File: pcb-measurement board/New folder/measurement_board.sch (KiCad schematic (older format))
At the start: 92 parts, among them P1 HDR DUAL ROW, P2 CONN_02X15, P3 CONN_02X13, P4 CONN_02X05, P5 CONN_02X05, Q1 Si1101X, U1 NX3L4051, U10 TLV1G125, U11 NX3L4051, U12 MSP430G2955, U13 AD8603, U14 TLV1G125, U15 MCP4921, U16 AD8293, U17 NX3L4051, U18 NX3L4051, U19 QS4A110, U2 TPS73133, U20 QS4A110, U21 TLV1G125, U22 TLV1G125, U3 74CBTLV3253, U4 NX3L4051, U5 TPS73125, U6 AD8603, U7 MCP4921, U8 NX3L4051, U9 TLV1G125

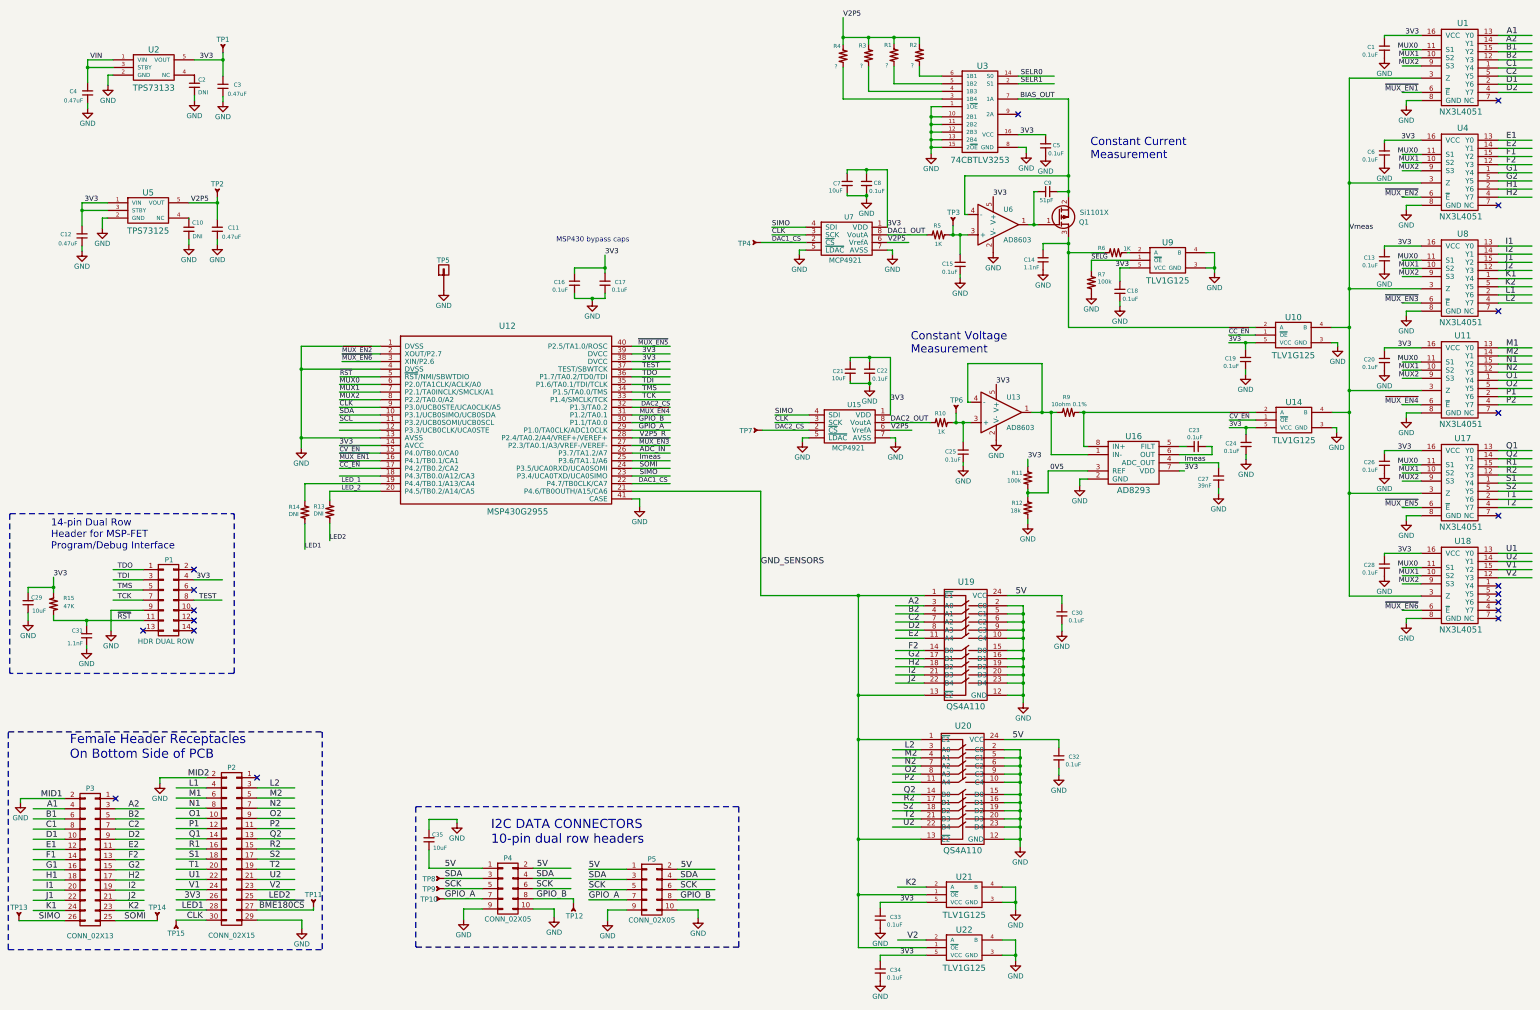
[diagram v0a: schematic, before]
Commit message: -replaced all measurement board 0402 components with 0603 -adjusted placement and started routing on the layout
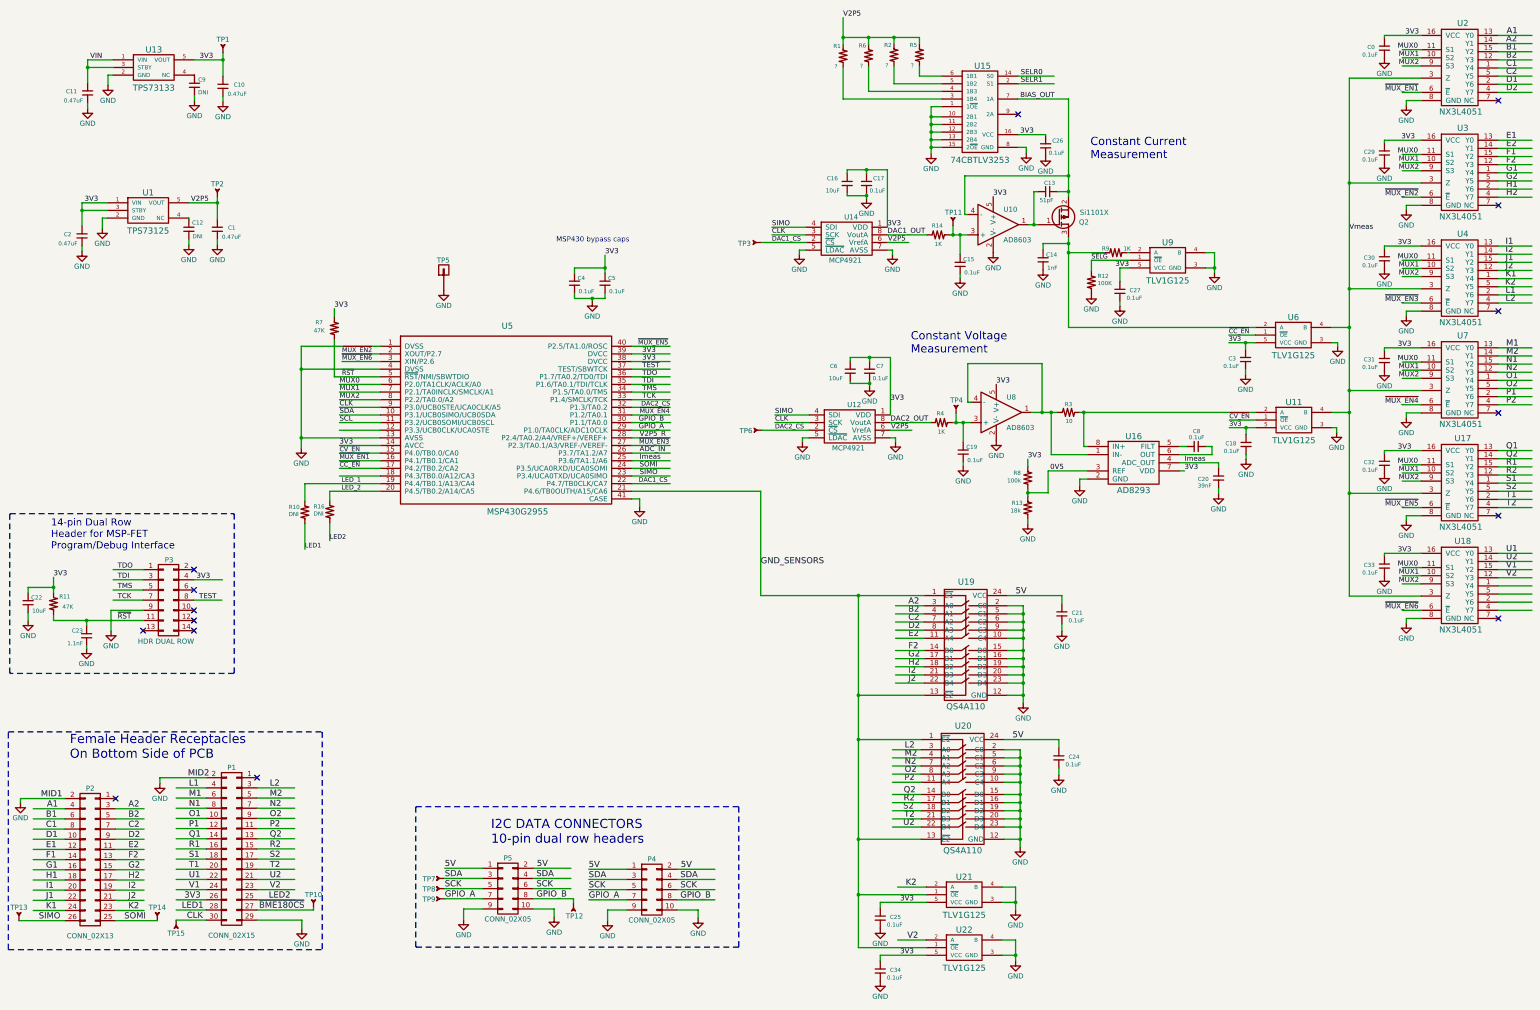
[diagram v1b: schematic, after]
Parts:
- removed C18, C22, C23, C25: 0.1uF, footprints_on_Cdrive:0603, symbol CAP_NP
- removed C21, C35: 10uF, footprints_on_Cdrive:0603, symbol CAP_NP
- removed R15: 47K, footprints_on_Cdrive:0603, symbol Res1_1
- removed R5, R6: 1K, footprints_on_Cdrive:0603, symbol Res1_1
- added C19, C26, C4: 0.1uF, footprints_on_Cdrive:0402, symbol CAP_NP
- added C27: 0.1uF, Resistors_SMD:R_0603_HandSoldering, symbol CAP_NP
- added C6: 10uF, footprints_on_Cdrive:0402, symbol CAP_NP
- added R11: 47K, footprints_on_Cdrive:0402, symbol Res1
- added R12: 100K, footprints_on_Cdrive:0402, symbol Res1_1
- added R14, R9: 1K, footprints_on_Cdrive:0402, symbol Res1_1
- C13: renamed from C9; footprint footprints_on_Cdrive:0603 -> footprints_on_Cdrive:0402; description CAP CER 51PF 50V C0G/NP0 0603 -> CAP CER 51PF 50V NP0 0402; manufacturer pn GRM1885C1H510JA01D -> GRM1555C1H510JA01D; supplier pn 490-1420-1-ND -> 490-5944-1-ND
- C14: value 1.1nF -> 1nF; footprint footprints_on_Cdrive:0603 -> footprints_on_Cdrive:0402; description CAP CER 1100PF 50V C0G/NP0 0603 -> CAP CER 1000PF 50V X7R 0402; manufacturer pn GRM1885C1H112JA01D -> GRM155R71H102KA01D; supplier pn 490-1452-1-ND -> 490-1303-1-ND
- C15, C17, C5, C8: footprint footprints_on_Cdrive:0603 -> footprints_on_Cdrive:0402; description CAP CER 0.1UF 16V X7R 0603 -> CAP CER 0.1UF 16V X5R 0402; manufacturer pn GRM188R71C104KA01D -> 0402YD104KAT2A; supplier pn 490-1532-1-ND -> 478-1126-1-ND
- C16: value 0.1uF -> 10uF; footprint footprints_on_Cdrive:0603 -> footprints_on_Cdrive:0402; description CAP CER 0.1UF 16V X7R 0603 -> CAP CER 10UF 10V X5R 0402; manufacturer AVX Corporation -> Samsung; manufacturer pn GRM188R71C104KA01D -> CL05A106MP8NUB8; supplier pn 490-1532-1-ND -> 1276-6830-1-ND
- C18: renamed from C24; footprint footprints_on_Cdrive:0603 -> Resistors_SMD:R_0603_HandSoldering
- C20: renamed from C27; footprint footprints_on_Cdrive:0603 -> footprints_on_Cdrive:0402; description CAP CER 0.039UF 16V X7R 0603 -> CAP CER 0.1UF 16V X5R 0402; manufacturer Kemet -> AVX Corporation; manufacturer pn C0603C393K4RACTU -> 0402YD104KAT2A; supplier pn 399-9078-1-ND -> 478-1126-1-ND
- C22: renamed from C29; footprint footprints_on_Cdrive:0603 -> footprints_on_Cdrive:0402; description CAP CER 10UF 6.3V X5R 0603 -> CAP CER 10UF 4V X5R 0402; manufacturer pn GRM188R60J106ME47D -> GRM155R60G106ME44D; supplier pn 490-3896-1-ND -> 490-10693-1-ND
- C23: renamed from C31; footprint footprints_on_Cdrive:0603 -> footprints_on_Cdrive:0402; description CAP CER 1100PF 50V C0G/NP0 0603 -> CAP CER 1100PF 50V NP0 0402; manufacturer Murata -> Kemet; manufacturer pn GRM1885C1H112JA01D -> C0402C112J5GAC7867; supplier pn 490-1452-1-ND -> 399-9948-1-ND
- C29: renamed from C6; footprint footprints_on_Cdrive:0603 -> Resistors_SMD:R_0603_HandSoldering
- C3: renamed from C19; footprint footprints_on_Cdrive:0603 -> Resistors_SMD:R_0603_HandSoldering
- C30: renamed from C13; footprint footprints_on_Cdrive:0603 -> Resistors_SMD:R_0603_HandSoldering
- C31: renamed from C20; footprint footprints_on_Cdrive:0603 -> Resistors_SMD:R_0603_HandSoldering
- C32: renamed from C26; footprint footprints_on_Cdrive:0603 -> Resistors_SMD:R_0603_HandSoldering
- C33: renamed from C28; footprint footprints_on_Cdrive:0603 -> Resistors_SMD:R_0603_HandSoldering
- C7: value 10uF -> 0.1uF; footprint footprints_on_Cdrive:0603 -> footprints_on_Cdrive:0402; description CAP CER 10UF 6.3V X5R 0603 -> CAP CER 0.1UF 16V X5R 0402; manufacturer Murata -> AVX Corporation; manufacturer pn GRM188R60J106ME47D -> 0402YD104KAT2A; supplier pn 490-3896-1-ND -> 478-1126-1-ND
- R13: renamed from R12; footprint footprints_on_Cdrive:0603 -> footprints_on_Cdrive:0402; description RES SMD 18K OHM 1% 1/10W 0603 -> RES SMD 100K OHM 1% 1/16W 0402; manufacturer Yageo -> Stackpole Electronics Inc.; manufacturer pn RC0603FR-0718KL -> RC0402FR-07100KL; supplier pn 311-18.0KHRCT-ND -> 311-100KLRCT-ND
- R3: renamed from R9; value 10ohm 0.1% -> 10; footprint footprints_on_Cdrive:0805 -> footprints_on_Cdrive:0402; description RES SMD 10 OHM 0.1% 1/4W 0805 -> RES SMD 100K OHM 1% 1/16W 0402; manufacturer TE Connectivity -> Stackpole Electronics Inc.; manufacturer pn 2-1625868-7 -> RC0402FR-07100KL; supplier pn A110351CT-ND -> 311-100KLRCT-ND
- R4: renamed from R10; footprint footprints_on_Cdrive:0603 -> footprints_on_Cdrive:0402; description RES SMD 1K OHM 1% 1/10W 0603 -> RES SMD 1K OHM 1% 1/16W 0402; manufacturer pn RC0603FR-071KLL -> RC0402FR-071KL; supplier pn 311-1.00KHRCT-ND -> 311-1.00KLRCT-ND
- R7: value 100k -> 47K; footprint footprints_on_Cdrive:0603 -> footprints_on_Cdrive:0402; description RES SMD 100K OHM 1% 1/10W 0603 -> RES SMD 47K OHM 1% 1/16W 0402; manufacturer Yageo -> Stackpole Electronics Inc.; manufacturer pn RC0603FR-07100KL -> RMCF0402FT47K0; supplier pn 311-100KHRCT-ND -> RMCF0402FT47K0CT-ND
- R8: renamed from R11; footprint footprints_on_Cdrive:0603 -> footprints_on_Cdrive:0402; description RES SMD 100K OHM 1% 1/10W 0603 -> RES SMD 100K OHM 1% 1/16W 0402; manufacturer Yageo -> Stackpole Electronics Inc.; manufacturer pn RC0603FR-07100KL -> RC0402FR-07100KL; supplier pn 311-100KHRCT-ND -> 311-100KLRCT-ND
- renumbered C1 to C0, C11 to C1, C3 to C10, C4 to C11, C10 to C12, C12 to C2, C30 to C21, C32 to C24, C33 to C25, C2 to C9, P2 to P1, P3 to P2, P1 to P3, P5 to P4, P4 to P5, Q1 to Q2, R4 to R1, R14 to R10, R13 to R16, R1 to R2, R2 to R5, R3 to R6, TP11 to TP10, TP3 to TP11, TP4 to TP3, TP6 to TP4, TP7 to TP6, TP8 to TP7, TP9 to TP8, TP10 to TP9, U5 to U1, U6 to U10, U14 to U11, U15 to U12, U2 to U13, U7 to U14, U3 to U15, U1 to U2, U4 to U3, U8 to U4, U12 to U5, U10 to U6, U11 to U7, U13 to U8
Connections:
- wire segments 476 -> 478
- no-connect marks 19 -> 15
